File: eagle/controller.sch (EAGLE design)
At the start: 12 parts, among them IC1 MAX7219CNG, IC2 ATMEGA328, X1 22-23-2031

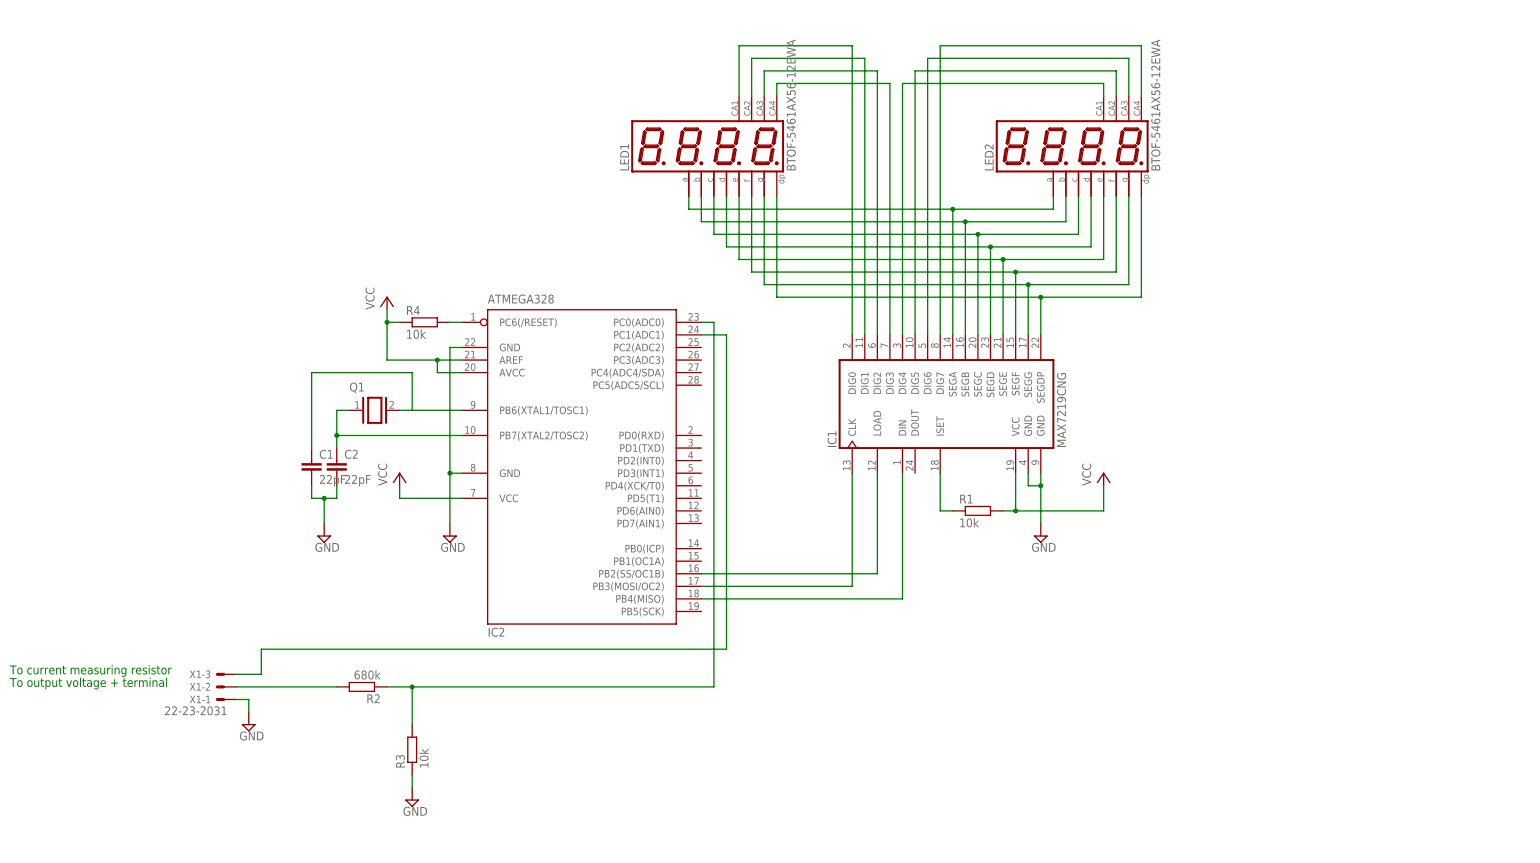
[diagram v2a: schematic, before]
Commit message: Added coarse/fine voltage regulation opamp circuit, moved things around Just needs rotary encoder/switches implemented
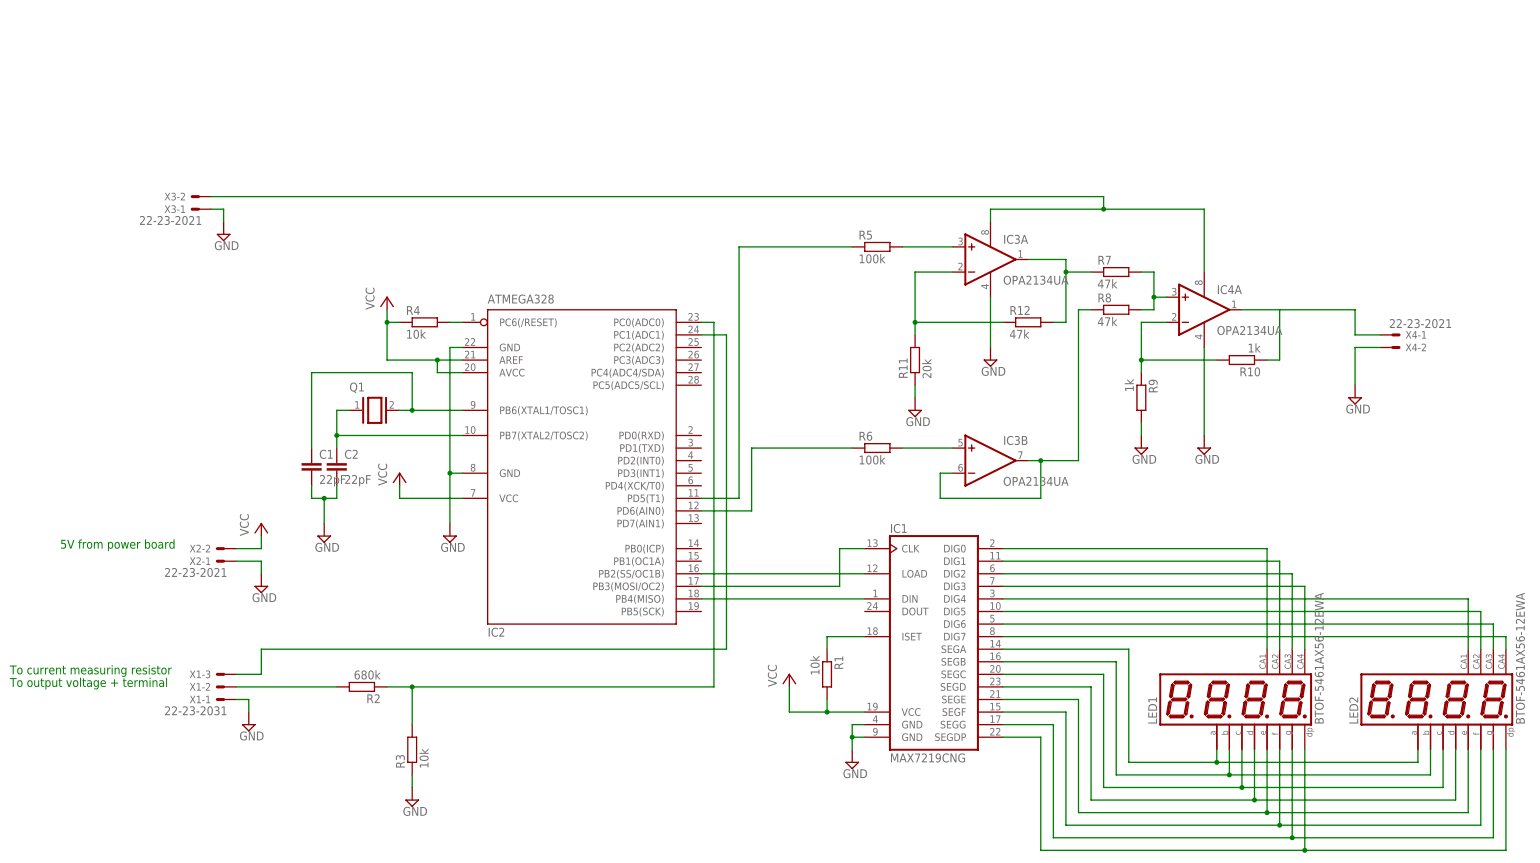
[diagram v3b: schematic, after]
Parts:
- added IC3, IC4: OPA2134UA, linear:OPA2134UA
- added R10, R9: 1k, rcl:R-EU_0207/10
- added R11: 20k, rcl:R-EU_0207/10
- added R12, R7, R8: 47k, rcl:R-EU_0207/10
- added R5, R6: 100k, rcl:R-EU_0207/10
- added X2, X3, X4: 22-23-2021, con-molex:22-23-2021
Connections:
- new net N$26: IC3B.-IN, IC3B.OUT, R8.1
- new net N$27: IC2.PD5(T1), R5.1
- new net N$29: IC3A.+IN, R5.2
- new net N$30: IC3B.+IN, R6.2
- new net N$31: IC3A.V+, IC4A.V+, X3-2.S
- new net N$32: IC2.PD6(AIN0), R6.1
- new net N$33: IC4A.+IN, R7.2, R8.2
- new net N$34: IC3A.OUT, R12.2, R7.1
- new net N$35: IC3A.-IN, R11.2, R12.1
- new net N$36: IC4A.-IN, R10.2, R9.1
- new net N$37: IC4A.OUT, R10.1, X4-1.S
- net GND: now also IC3A.V-, IC4A.V-, R11.1, R9.2, X2-1.S, X3-1.S, X4-2.S
- net VCC: now also X2-2.S
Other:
- note added: "5V from power board"
- moved on the sheet: IC1, LED1, LED2, R1

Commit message: Finished schematic
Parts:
- added C3, C4, C5, C6: 100nF, capacitor-wima:C7.5/3
- added D1: BZX-85C3V9, diode:BZX90
- added SW1, SW2: EC12E_SW, switch-alps:EC12E_SW
- IC3, IC4: value OPA2134UA -> LT1490AIS8
- Q1: value (none) -> 16MHz
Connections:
- new net N$38: IC2.PB1(OC1A), SW2G$2.2
- new net N$39: IC2.PB0(ICP), SW1G$2.2
- new net N$40: IC2.PC2(ADC2), SW1G$1.B
- new net N$41: IC2.PC5(ADC5/SCL), SW2G$1.A
- new net N$42: IC2.PC4(ADC4/SDA), SW2G$1.B
- new net N$43: D1.C, X3-2.S
- new net N$45: IC2.PC3(ADC3), SW1G$1.A
- net GND: now also C3.2, C4.2, C5.2, C6.2, SW1G$1.C, SW1G$2.1, SW2G$1.C, SW2G$2.1
- net N$29: now also C3.1
- net N$30: now also C4.1
- net N$31: now also C5.1, C6.1, D1.A; no longer X3-2.S
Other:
- note added: "From current measuring resistor on power board"
- note added: "From output voltage + terminal"
- note added: "Raw rectified, flattened voltage, about 47V"
- note added: "To LM317HV Voltage adjust on power board"
- note removed: "To current measuring resistor"
- note removed: "To output voltage + terminal"
- moved on the sheet: IC1, IC3A, IC3B, IC4A, LED1, LED2, R1, R10, R11, R12, R5, R6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
